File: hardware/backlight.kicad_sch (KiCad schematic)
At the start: 40 parts, among them U4 74HCT1G125GW

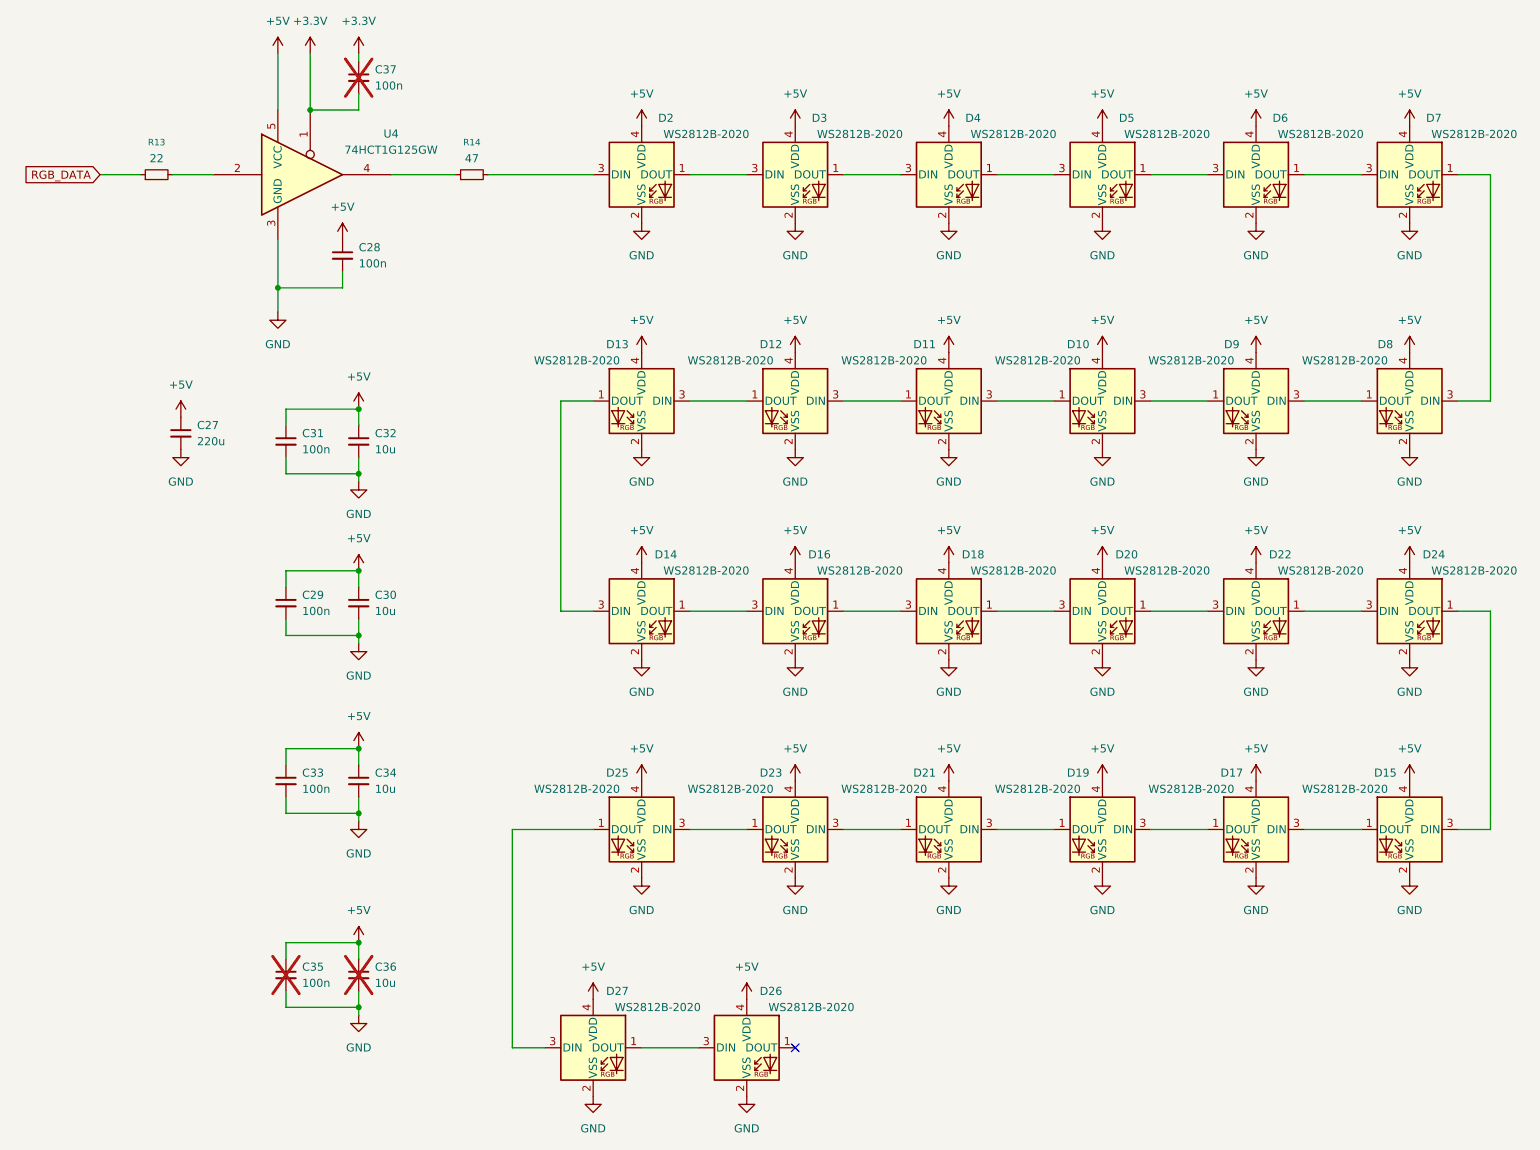
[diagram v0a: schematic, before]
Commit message: separate left/right part design, schematic
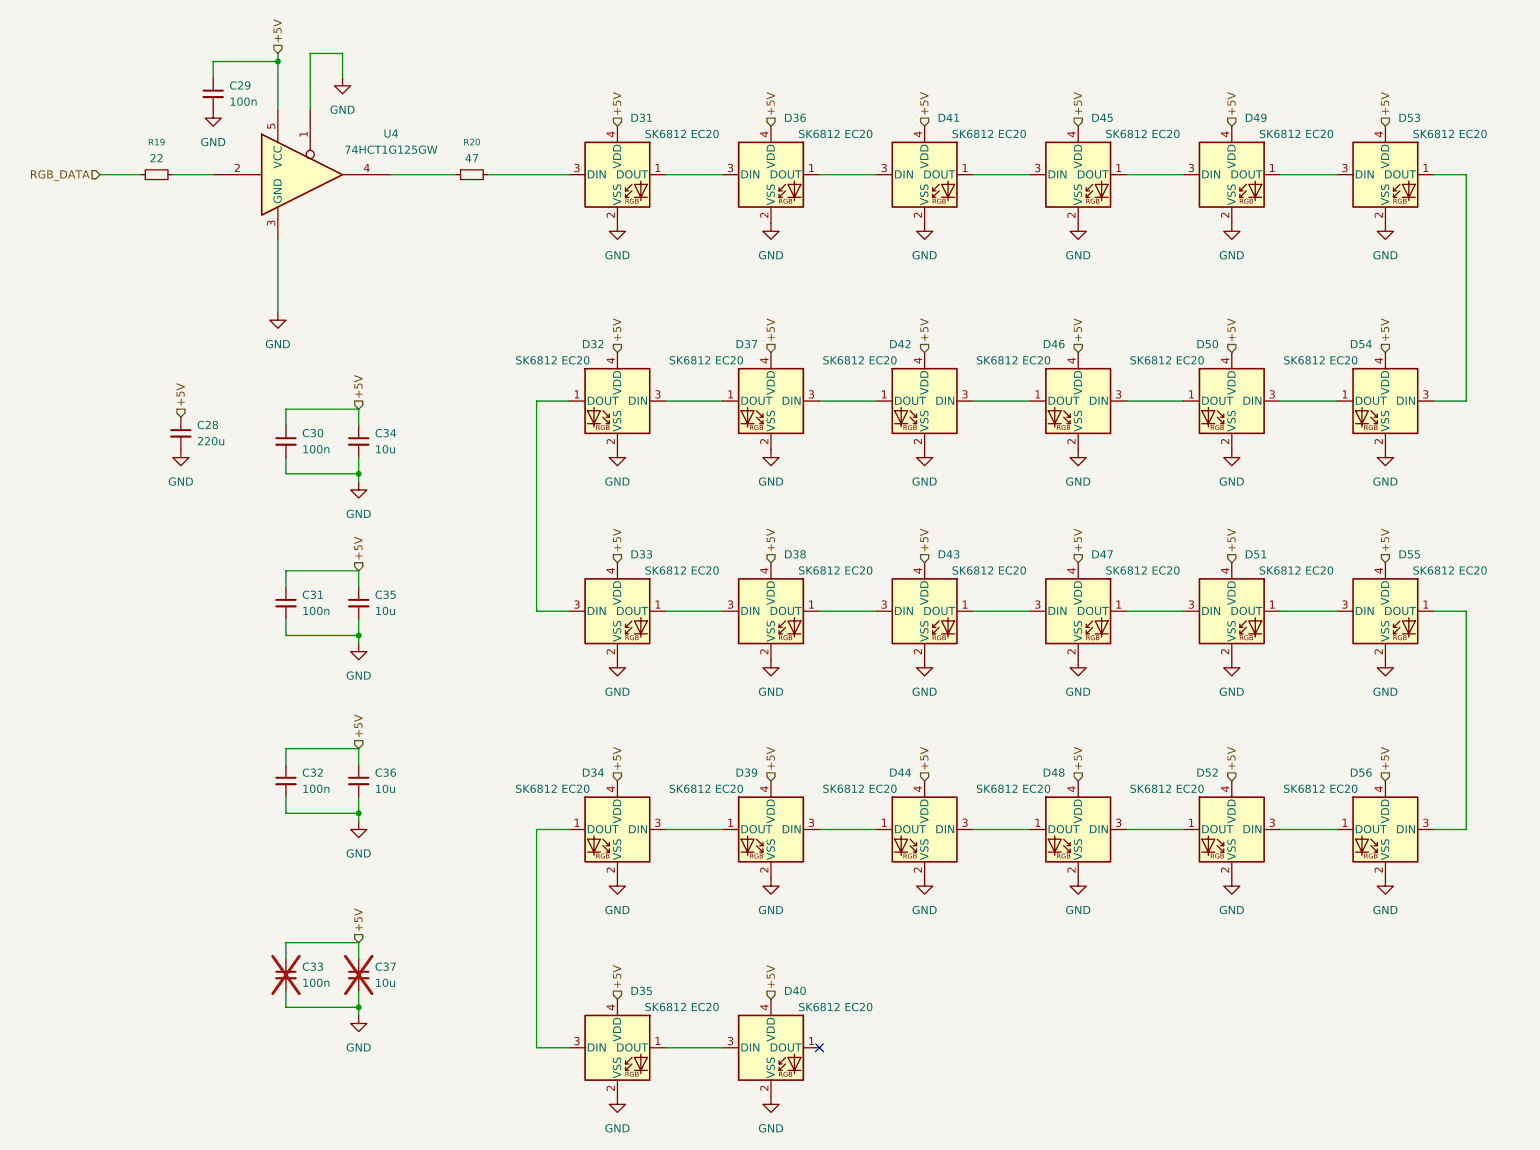
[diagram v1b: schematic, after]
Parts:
- removed C28, C37: 100n, PCM_Capacitor_SMD_AKL:C_0603_1608Metric_Pad1.05x0.95mm_HandSolder, symbol Device:C_Small
- added C29: 100n, PCM_Capacitor_SMD_AKL:C_0603_1608Metric_Pad1.05x0.95mm_HandSolder, symbol Device:C_Small
- D31: renamed from D2; value WS2812B-2020 -> SK6812 EC20; footprint LED_SMD:LED_WS2812B-2020_PLCC4_2.0x2.0mm -> rp_voyager:LED_SK6812_EC20_2x2mm
- D32: renamed from D8; value WS2812B-2020 -> SK6812 EC20; footprint LED_SMD:LED_WS2812B-2020_PLCC4_2.0x2.0mm -> rp_voyager:LED_SK6812_EC20_2x2mm
- D33: renamed from D14; value WS2812B-2020 -> SK6812 EC20; footprint LED_SMD:LED_WS2812B-2020_PLCC4_2.0x2.0mm -> rp_voyager:LED_SK6812_EC20_2x2mm
- D34: renamed from D15; value WS2812B-2020 -> SK6812 EC20; footprint LED_SMD:LED_WS2812B-2020_PLCC4_2.0x2.0mm -> rp_voyager:LED_SK6812_EC20_2x2mm
- D35: renamed from D27; value WS2812B-2020 -> SK6812 EC20; footprint LED_SMD:LED_WS2812B-2020_PLCC4_2.0x2.0mm -> rp_voyager:LED_SK6812_EC20_2x2mm
- D36: renamed from D3; value WS2812B-2020 -> SK6812 EC20; footprint LED_SMD:LED_WS2812B-2020_PLCC4_2.0x2.0mm -> rp_voyager:LED_SK6812_EC20_2x2mm
- D37: renamed from D9; value WS2812B-2020 -> SK6812 EC20; footprint LED_SMD:LED_WS2812B-2020_PLCC4_2.0x2.0mm -> rp_voyager:LED_SK6812_EC20_2x2mm
- D38: renamed from D16; value WS2812B-2020 -> SK6812 EC20; footprint LED_SMD:LED_WS2812B-2020_PLCC4_2.0x2.0mm -> rp_voyager:LED_SK6812_EC20_2x2mm
- D39: renamed from D17; value WS2812B-2020 -> SK6812 EC20; footprint LED_SMD:LED_WS2812B-2020_PLCC4_2.0x2.0mm -> rp_voyager:LED_SK6812_EC20_2x2mm
- D40: renamed from D26; value WS2812B-2020 -> SK6812 EC20; footprint LED_SMD:LED_WS2812B-2020_PLCC4_2.0x2.0mm -> rp_voyager:LED_SK6812_EC20_2x2mm
- D41: renamed from D4; value WS2812B-2020 -> SK6812 EC20; footprint LED_SMD:LED_WS2812B-2020_PLCC4_2.0x2.0mm -> rp_voyager:LED_SK6812_EC20_2x2mm
- D42: renamed from D10; value WS2812B-2020 -> SK6812 EC20; footprint LED_SMD:LED_WS2812B-2020_PLCC4_2.0x2.0mm -> rp_voyager:LED_SK6812_EC20_2x2mm
- D43: renamed from D18; value WS2812B-2020 -> SK6812 EC20; footprint LED_SMD:LED_WS2812B-2020_PLCC4_2.0x2.0mm -> rp_voyager:LED_SK6812_EC20_2x2mm
- D44: renamed from D19; value WS2812B-2020 -> SK6812 EC20; footprint LED_SMD:LED_WS2812B-2020_PLCC4_2.0x2.0mm -> rp_voyager:LED_SK6812_EC20_2x2mm
- D45: renamed from D5; value WS2812B-2020 -> SK6812 EC20; footprint LED_SMD:LED_WS2812B-2020_PLCC4_2.0x2.0mm -> rp_voyager:LED_SK6812_EC20_2x2mm
- D46: renamed from D11; value WS2812B-2020 -> SK6812 EC20; footprint LED_SMD:LED_WS2812B-2020_PLCC4_2.0x2.0mm -> rp_voyager:LED_SK6812_EC20_2x2mm
- D47: renamed from D20; value WS2812B-2020 -> SK6812 EC20; footprint LED_SMD:LED_WS2812B-2020_PLCC4_2.0x2.0mm -> rp_voyager:LED_SK6812_EC20_2x2mm
- D48: renamed from D21; value WS2812B-2020 -> SK6812 EC20; footprint LED_SMD:LED_WS2812B-2020_PLCC4_2.0x2.0mm -> rp_voyager:LED_SK6812_EC20_2x2mm
- D49: renamed from D6; value WS2812B-2020 -> SK6812 EC20; footprint LED_SMD:LED_WS2812B-2020_PLCC4_2.0x2.0mm -> rp_voyager:LED_SK6812_EC20_2x2mm
- D50: renamed from D12; value WS2812B-2020 -> SK6812 EC20; footprint LED_SMD:LED_WS2812B-2020_PLCC4_2.0x2.0mm -> rp_voyager:LED_SK6812_EC20_2x2mm
- D51: renamed from D22; value WS2812B-2020 -> SK6812 EC20; footprint LED_SMD:LED_WS2812B-2020_PLCC4_2.0x2.0mm -> rp_voyager:LED_SK6812_EC20_2x2mm
- D52: renamed from D23; value WS2812B-2020 -> SK6812 EC20; footprint LED_SMD:LED_WS2812B-2020_PLCC4_2.0x2.0mm -> rp_voyager:LED_SK6812_EC20_2x2mm
- D53: renamed from D7; value WS2812B-2020 -> SK6812 EC20; footprint LED_SMD:LED_WS2812B-2020_PLCC4_2.0x2.0mm -> rp_voyager:LED_SK6812_EC20_2x2mm
- D54: renamed from D13; value WS2812B-2020 -> SK6812 EC20; footprint LED_SMD:LED_WS2812B-2020_PLCC4_2.0x2.0mm -> rp_voyager:LED_SK6812_EC20_2x2mm
- D55: renamed from D24; value WS2812B-2020 -> SK6812 EC20; footprint LED_SMD:LED_WS2812B-2020_PLCC4_2.0x2.0mm -> rp_voyager:LED_SK6812_EC20_2x2mm
- D56: renamed from D25; value WS2812B-2020 -> SK6812 EC20; footprint LED_SMD:LED_WS2812B-2020_PLCC4_2.0x2.0mm -> rp_voyager:LED_SK6812_EC20_2x2mm
- R19: renamed from R13; footprint Resistor_SMD:R_0603_1608Metric_Pad0.98x0.95mm_HandSolder -> PCM_Resistor_SMD_AKL:R_0603_1608Metric_Pad0.98x0.95mm_HandSolder
- R20: renamed from R14; footprint Resistor_SMD:R_0603_1608Metric_Pad0.98x0.95mm_HandSolder -> PCM_Resistor_SMD_AKL:R_0603_1608Metric_Pad0.98x0.95mm_HandSolder
- renumbered C27 to C28, C31 to C30, C29 to C31, C33 to C32, C35 to C33, C32 to C34, C30 to C35, C34 to C36, C36 to C37
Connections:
- net +3.3V is gone; now on net GND: U4.1
- net +5V: now also C29.1
- net GND: now also C29.2
- net at D35.3 (DIN): now also D34.1 (DOUT); no longer D56.1 (DOUT)
- net at D32.1 (DOUT): now also D33.3 (DIN); no longer D37.3 (DIN)
- net at D32.3 (DIN): now also D37.1 (DOUT); no longer D53.1 (DOUT)
- net at D54.1 (DOUT): now also D50.3 (DIN); no longer D33.3 (DIN)
- net at D54.3 (DIN): now also D53.1 (DOUT); no longer D50.1 (DOUT)
- net at D42.3 (DIN): now also D46.1 (DOUT); no longer D37.1 (DOUT)
- net at D42.1 (DOUT): now also D37.3 (DIN); no longer D46.3 (DIN)
- net at D39.1 (DOUT): now also D34.3 (DIN); no longer D44.3 (DIN)
- net at D39.3 (DIN): now also D44.1 (DOUT); no longer D34.1 (DOUT)
- net at D55.1 (DOUT): now also D56.3 (DIN); no longer D34.3 (DIN)
- net at D48.3 (DIN): now also D52.1 (DOUT); no longer D44.1 (DOUT)
- net at D48.1 (DOUT): now also D44.3 (DIN); no longer D52.3 (DIN)
- new net: D46.3 (DIN), D50.1 (DOUT)
- new net: D52.3 (DIN), D56.1 (DOUT)
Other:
- moved on the sheet: D31, D32, D33, D34, D35, D36, D37, D38, D39, D40, D41, D42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

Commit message: electronics
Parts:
- C26: renamed from C28; footprint PCM_Capacitor_SMD_AKL:C_1210_3225Metric_Pad1.33x2.70mm_HandSolder -> PCM_Capacitor_SMD_Handsoldering_AKL:C_1210_3225Metric
- C27: renamed from C29; footprint PCM_Capacitor_SMD_AKL:C_0603_1608Metric_Pad1.05x0.95mm_HandSolder -> PCM_Capacitor_SMD_Handsoldering_AKL:C_0603_1608Metric; Distributor Link 3 (none) -> https://www.hestore.hu/prod_10033461.html
- C28: renamed from C30; footprint PCM_Capacitor_SMD_AKL:C_0603_1608Metric_Pad1.05x0.95mm_HandSolder -> PCM_Capacitor_SMD_Handsoldering_AKL:C_0603_1608Metric; Distributor Link 3 (none) -> https://www.hestore.hu/prod_10033461.html
- C29: renamed from C31; footprint PCM_Capacitor_SMD_AKL:C_0603_1608Metric_Pad1.05x0.95mm_HandSolder -> PCM_Capacitor_SMD_Handsoldering_AKL:C_0603_1608Metric; Distributor Link 3 (none) -> https://www.hestore.hu/prod_10033461.html
- C30: renamed from C32; footprint PCM_Capacitor_SMD_AKL:C_0603_1608Metric_Pad1.05x0.95mm_HandSolder -> PCM_Capacitor_SMD_Handsoldering_AKL:C_0603_1608Metric; Distributor Link 3 (none) -> https://www.hestore.hu/prod_10033461.html
- C31: renamed from C33; footprint PCM_Capacitor_SMD_AKL:C_0603_1608Metric_Pad1.05x0.95mm_HandSolder -> PCM_Capacitor_SMD_Handsoldering_AKL:C_0603_1608Metric
- C32: renamed from C34; footprint PCM_Capacitor_SMD_AKL:C_0805_2012Metric_Pad1.15x1.40mm_HandSolder -> PCM_Capacitor_SMD_Handsoldering_AKL:C_0805_2012Metric; Distributor Link 1 (none) -> https://hu.mouser.com/ProductDetail/KEMET/C0805C106M8RACAUT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
- C33: renamed from C35; footprint PCM_Capacitor_SMD_AKL:C_0805_2012Metric_Pad1.15x1.40mm_HandSolder -> PCM_Capacitor_SMD_Handsoldering_AKL:C_0805_2012Metric; Distributor Link 1 (none) -> https://hu.mouser.com/ProductDetail/KEMET/C0805C106M8RACAUT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
- C34: renamed from C36; footprint PCM_Capacitor_SMD_AKL:C_0805_2012Metric_Pad1.15x1.40mm_HandSolder -> PCM_Capacitor_SMD_Handsoldering_AKL:C_0805_2012Metric; Distributor Link 1 (none) -> https://hu.mouser.com/ProductDetail/KEMET/C0805C106M8RACAUT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
- C35: renamed from C37; footprint PCM_Capacitor_SMD_AKL:C_0805_2012Metric_Pad1.15x1.40mm_HandSolder -> PCM_Capacitor_SMD_Handsoldering_AKL:C_0805_2012Metric
- R17: renamed from R19; footprint PCM_Resistor_SMD_AKL:R_0603_1608Metric_Pad0.98x0.95mm_HandSolder -> PCM_Resistor_SMD_AKL:R_0603_1608Metric; Distributor Link 3 (none) -> https://www.hestore.hu/prod_10023927.html
- R18: renamed from R20; footprint PCM_Resistor_SMD_AKL:R_0603_1608Metric_Pad0.98x0.95mm_HandSolder -> PCM_Resistor_SMD_AKL:R_0603_1608Metric; Distributor Link 3 (none) -> https://www.hestore.hu/prod_10049205.html
